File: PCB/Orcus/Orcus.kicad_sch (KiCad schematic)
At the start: 78 parts, among them SW1 MX_LED, SW10 MX_LED, SW11 MX_LED, SW12 MX_LED, SW13 MX_LED, SW14 MX_LED, SW15 MX_LED, SW16 MX_LED, SW17 MX_LED, SW18 MX_LED, SW19 MX_LED, SW2 MX_LED, SW20 MX_LED, SW21 MX_LED, SW22 MX_LED, SW23 MX_LED, SW24 MX_LED, SW25 MX_LED, SW26 MX_LED, SW27 MX_LED, SW28 MX_LED, SW29 MX_LED, SW3 MX_LED, SW30 MX_LED, SW31 MX_LED, SW32 MX_LED, SW33 MX_LED, SW34 MX_LED, SW35 MX_LED, SW36 MX_LED, SW37 MX_LED, SW38 MX_LED, SW4 MX_LED, SW5 MX_LED, SW6 MX_LED, SW7 MX_LED, SW8 MX_LED, SW9 MX_LED, U1 SeeeduinoXIAO, U2 SeeeduinoXIAO

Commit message: update sch
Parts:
- SW1, SW10, SW11, SW12, SW13, SW14, SW15, SW16, SW17, SW18, SW19, SW2, SW20, SW21, SW22, SW23, SW24, SW25, SW26, SW27, SW28, SW29, SW3, SW30, SW31, SW32, SW33, SW34, SW35, SW36, SW37, SW38, SW4, SW5, SW6, SW7, SW8, SW9: footprint Keebio-Parts.pretty-master:Kailh-PG1350-1u-NoLED -> keyswitches.pretty-master:Kailh_socket_PG1350
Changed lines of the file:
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@@
 			)
 		)
-		(property "Footprint" "Keebio-Parts.pretty-master:Kailh-PG1350-1u-NoLED"
+		(property "Footprint" "keyswitches.pretty-master:Kailh_socket_PG1350"
 			(at 53.34 53.34 0)
 			(effects
@@
 			)
 		)
-		(property "Footprint" "Keebio-Parts.pretty-master:Kailh-PG1350-1u-NoLED"
+		(property "Footprint" "keyswitches.pretty-master:Kailh_socket_PG1350"
 			(at 93.98 161.29 0)
 			(effects
@@
 			)
 		)
-		(property "Footprint" "Keebio-Parts.pretty-master:Kailh-PG1350-1u-NoLED"
+		(property "Footprint" "keyswitches.pretty-master:Kailh_socket_PG1350"
 			(at 53.34 35.56 0)
 			(effects
@@
 			)
 		)
-		(property "Footprint" "Keebio-Parts.pretty-master:Kailh-PG1350-1u-NoLED"
+		(property "Footprint" "keyswitches.pretty-master:Kailh_socket_PG1350"
 			(at 74.93 161.29 0)
 			(effects
@@
 			)
 		)
-		(property "Footprint" "Keebio-Parts.pretty-master:Kailh-PG1350-1u-NoLED"
+		(property "Footprint" "keyswitches.pretty-master:Kailh_socket_PG1350"
 			(at 113.03 161.29 0)
 			(effects
@@
 			)
 		)
-		(property "Footprint" "Keebio-Parts.pretty-master:Kailh-PG1350-1u-NoLED"
+		(property "Footprint" "keyswitches.pretty-master:Kailh_socket_PG1350"
 			(at 151.13 142.24 0)
 			(effects
@@
 			)
 		)
-		(property "Footprint" "Keebio-Parts.pretty-master:Kailh-PG1350-1u-NoLED"
+		(property "Footprint" "keyswitches.pretty-master:Kailh_socket_PG1350"
 			(at 130.81 124.46 0)
 			(effects
@@
 			)
 		)
-		(property "Footprint" "Keebio-Parts.pretty-master:Kailh-PG1350-1u-NoLED"
+		(property "Footprint" "keyswitches.pretty-master:Kailh_socket_PG1350"
 			(at 73.66 72.39 0)
 			(effects
@@
 			)
 		)
-		(property "Footprint" "Keebio-Parts.pretty-master:Kailh-PG1350-1u-NoLED"
+		(property "Footprint" "keyswitches.pretty-master:Kailh_socket_PG1350"
 			(at 36.83 181.61 0)
 			(effects
@@
 			)
 		)
-		(property "Footprint" "Keebio-Parts.pretty-master:Kailh-PG1350-1u-NoLED"
+		(property "Footprint" "keyswitches.pretty-master:Kailh_socket_PG1350"
 			(at 147.32 91.44 0)
 			(effects
@@
 			)
 		)
-		(property "Footprint" "Keebio-Parts.pretty-master:Kailh-PG1350-1u-NoLED"
+		(property "Footprint" "keyswitches.pretty-master:Kailh_socket_PG1350"
 			(at 93.98 142.24 0)
 			(effects
@@
 			)
 		)
-		(property "Footprint" "Keebio-Parts.pretty-master:Kailh-PG1350-1u-NoLED"
+		(property "Footprint" "keyswitches.pretty-master:Kailh_socket_PG1350"
 			(at 129.54 35.56 0)
 			(effects
@@
 			)
 		)
-		(property "Footprint" "Keebio-Parts.pretty-master:Kailh-PG1350-1u-NoLED"
+		(property "Footprint" "keyswitches.pretty-master:Kailh_socket_PG1350"
 			(at 111.76 35.56 0)
 			(effects
@@
 			)
 		)
-		(property "Footprint" "Keebio-Parts.pretty-master:Kailh-PG1350-1u-NoLED"
+		(property "Footprint" "keyswitches.pretty-master:Kailh_socket_PG1350"
 			(at 111.76 53.34 0)
 			(effects
@@
 			)
 		)
-		(property "Footprint" "Keebio-Parts.pretty-master:Kailh-PG1350-1u-NoLED"
+		(property "Footprint" "keyswitches.pretty-master:Kailh_socket_PG1350"
 			(at 113.03 142.24 0)
 			(effects
@@
 			)
 		)
-		(property "Footprint" "Keebio-Parts.pretty-master:Kailh-PG1350-1u-NoLED"
+		(property "Footprint" "keyswitches.pretty-master:Kailh_socket_PG1350"
 			(at 129.54 91.44 0)
 			(effects
@@
 			)
 		)
-		(property "Footprint" "Keebio-Parts.pretty-master:Kailh-PG1350-1u-NoLED"
+		(property "Footprint" "keyswitches.pretty-master:Kailh_socket_PG1350"
 			(at 129.54 53.34 0)
 			(effects
@@
 			)
 		)
-		(property "Footprint" "Keebio-Parts.pretty-master:Kailh-PG1350-1u-NoLED"
+		(property "Footprint" "keyswitches.pretty-master:Kailh_socket_PG1350"
 			(at 92.71 72.39 0)
 			(effects
@@
 			)
 		)
-		(property "Footprint" "Keebio-Parts.pretty-master:Kailh-PG1350-1u-NoLED"
+		(property "Footprint" "keyswitches.pretty-master:Kailh_socket_PG1350"
 			(at 31.75 53.34 0)
 			(effects
@@
 			)
 		)
-		(property "Footprint" "Keebio-Parts.pretty-master:Kailh-PG1350-1u-NoLED"
+		(property "Footprint" "keyswitches.pretty-master:Kailh_socket_PG1350"
 			(at 111.76 72.39 0)
 			(effects
@@
 			)
 		)
-		(property "Footprint" "Keebio-Parts.pretty-master:Kailh-PG1350-1u-NoLED"
+		(property "Footprint" "keyswitches.pretty-master:Kailh_socket_PG1350"
 			(at 130.81 161.29 0)
 			(effects
@@
 			)
 		)
-		(property "Footprint" "Keebio-Parts.pretty-master:Kailh-PG1350-1u-NoLED"
+		(property "Footprint" "keyswitches.pretty-master:Kailh_socket_PG1350"
 			(at 129.54 72.39 0)
 			(effects
@@
 			)
 		)
-		(property "Footprint" "Keebio-Parts.pretty-master:Kailh-PG1350-1u-NoLED"
+		(property "Footprint" "keyswitches.pretty-master:Kailh_socket_PG1350"
 			(at 111.76 91.44 0)
 			(effects
@@
 			)
 		)
-		(property "Footprint" "Keebio-Parts.pretty-master:Kailh-PG1350-1u-NoLED"
+		(property "Footprint" "keyswitches.pretty-master:Kailh_socket_PG1350"
 			(at 73.66 35.56 0)
 			(effects
@@
 			)
 		)
-		(property "Footprint" "Keebio-Parts.pretty-master:Kailh-PG1350-1u-NoLED"
+		(property "Footprint" "keyswitches.pretty-master:Kailh_socket_PG1350"
 			(at 72.39 181.61 0)
 			(effects
@@
 			)
 		)
-		(property "Footprint" "Keebio-Parts.pretty-master:Kailh-PG1350-1u-NoLED"
+		(property "Footprint" "keyswitches.pretty-master:Kailh_socket_PG1350"
 			(at 54.61 181.61 0)
 			(effects
@@
 			)
 		)
-		(property "Footprint" "Keebio-Parts.pretty-master:Kailh-PG1350-1u-NoLED"
+		(property "Footprint" "keyswitches.pretty-master:Kailh_socket_PG1350"
 			(at 93.98 124.46 0)
 			(effects
@@
 			)
 		)
-		(property "Footprint" "Keebio-Parts.pretty-master:Kailh-PG1350-1u-NoLED"
+		(property "Footprint" "keyswitches.pretty-master:Kailh_socket_PG1350"
 			(at 54.61 124.46 0)
 			(effects
@@
 			)
 		)
-		(property "Footprint" "Keebio-Parts.pretty-master:Kailh-PG1350-1u-NoLED"
+		(property "Footprint" "keyswitches.pretty-master:Kailh_socket_PG1350"
 			(at 54.61 161.29 0)
 			(effects
@@
 			)
 		)
-		(property "Footprint" "Keebio-Parts.pretty-master:Kailh-PG1350-1u-NoLED"
+		(property "Footprint" "keyswitches.pretty-master:Kailh_socket_PG1350"
 			(at 74.93 124.46 0)
 			(effects
@@
 			)
 		)
-		(property "Footprint" "Keebio-Parts.pretty-master:Kailh-PG1350-1u-NoLED"
+		(property "Footprint" "keyswitches.pretty-master:Kailh_socket_PG1350"
 			(at 113.03 124.46 0)
 			(effects
@@
 			)
 		)
-		(property "Footprint" "Keebio-Parts.pretty-master:Kailh-PG1350-1u-NoLED"
+		(property "Footprint" "keyswitches.pretty-master:Kailh_socket_PG1350"
 			(at 92.71 53.34 0)
 			(effects
@@
 			)
 		)
-		(property "Footprint" "Keebio-Parts.pretty-master:Kailh-PG1350-1u-NoLED"
+		(property "Footprint" "keyswitches.pretty-master:Kailh_socket_PG1350"
 			(at 130.81 142.24 0)
 			(effects
@@
 			)
 		)
-		(property "Footprint" "Keebio-Parts.pretty-master:Kailh-PG1350-1u-NoLED"
+		(property "Footprint" "keyswitches.pretty-master:Kailh_socket_PG1350"
 			(at 92.71 35.56 0)
 			(effects
@@
 			)
 		)
-		(property "Footprint" "Keebio-Parts.pretty-master:Kailh-PG1350-1u-NoLED"
+		(property "Footprint" "keyswitches.pretty-master:Kailh_socket_PG1350"
 			(at 53.34 72.39 0)
 			(effects
@@
 			)
 		)
-		(property "Footprint" "Keebio-Parts.pretty-master:Kailh-PG1350-1u-NoLED"
+		(property "Footprint" "keyswitches.pretty-master:Kailh_socket_PG1350"
 			(at 73.66 53.34 0)
 			(effects
@@
 			)
 		)
-		(property "Footprint" "Keebio-Parts.pretty-master:Kailh-PG1350-1u-NoLED"
+		(property "Footprint" "keyswitches.pretty-master:Kailh_socket_PG1350"
 			(at 54.61 142.24 0)
 			(effects
@@
 			)
 		)
-		(property "Footprint" "Keebio-Parts.pretty-master:Kailh-PG1350-1u-NoLED"
+		(property "Footprint" "keyswitches.pretty-master:Kailh_socket_PG1350"
 			(at 74.93 142.24 0)
 			(effects

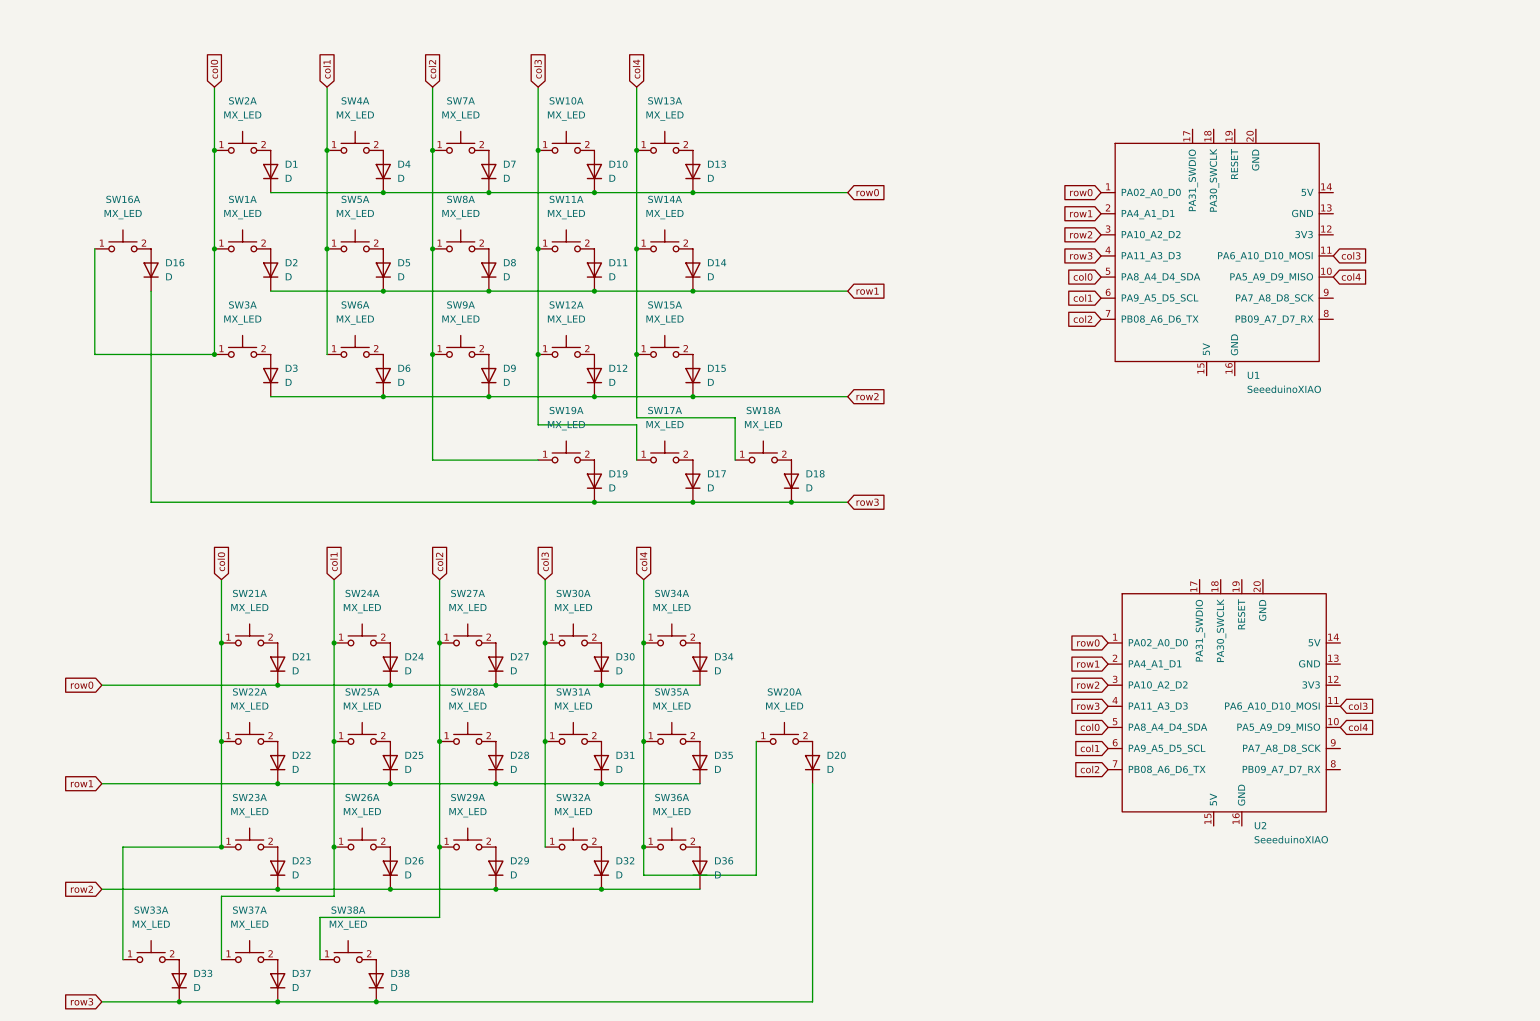
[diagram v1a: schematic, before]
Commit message: footprint laid out
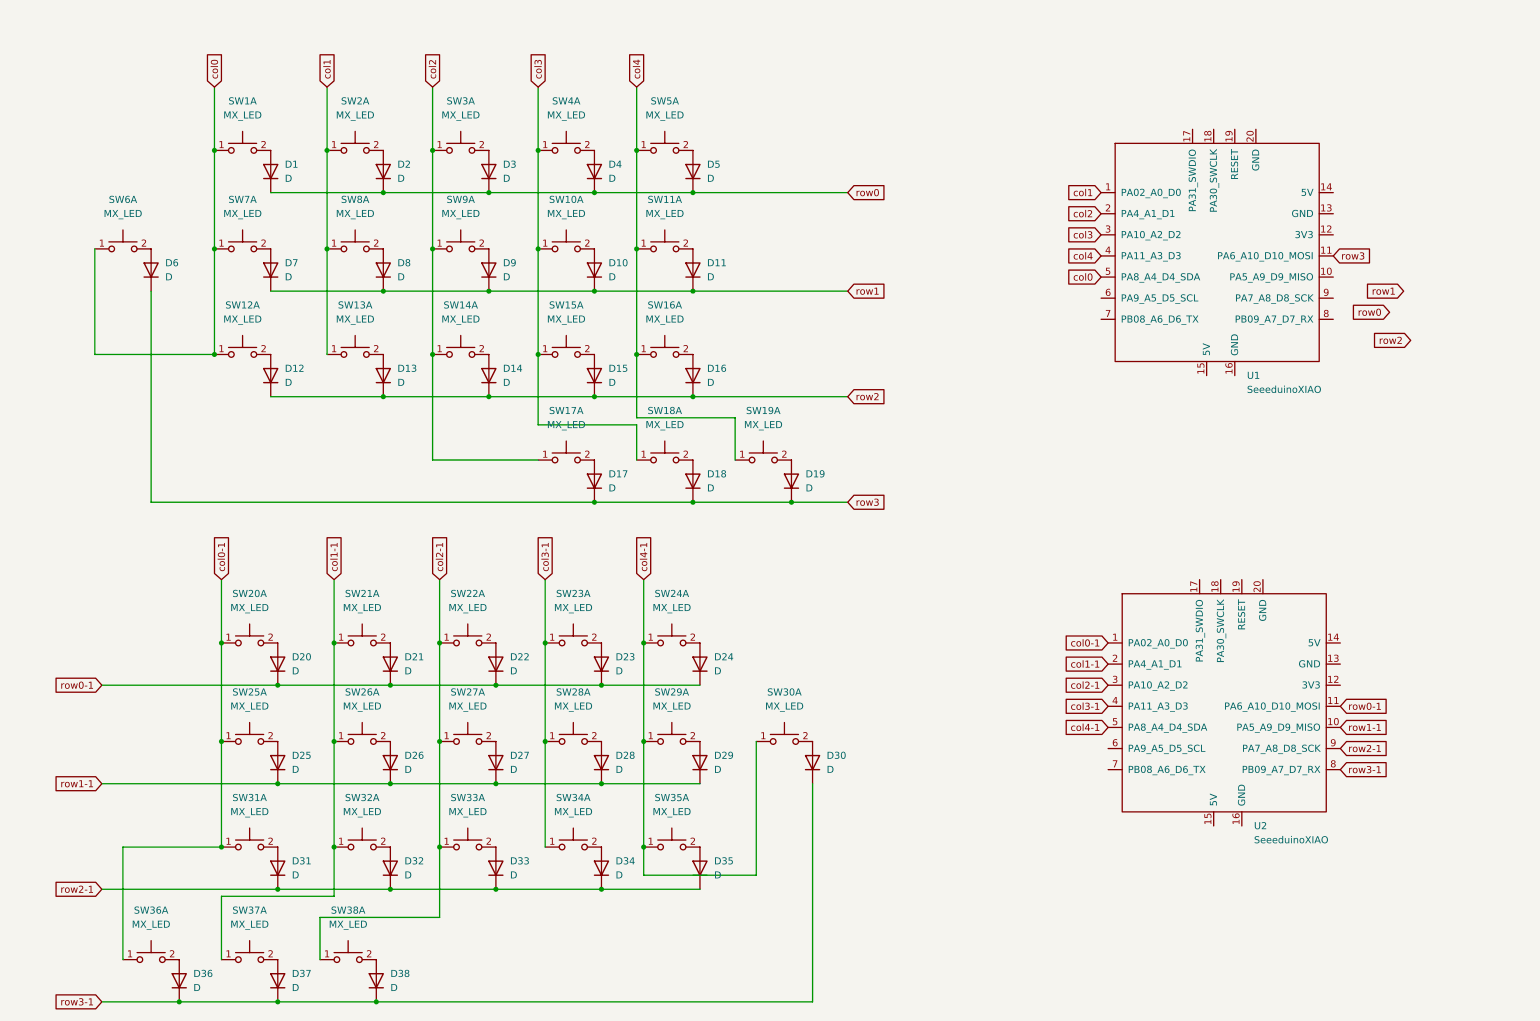
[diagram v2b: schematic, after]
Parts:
- D1, D37, D38: footprint Keebio-Parts.pretty-master:D_SOD123 -> Keebio-Parts.pretty-master:D_SOD123-Hole
- D10: renamed from D11; footprint Keebio-Parts.pretty-master:D_SOD123 -> Keebio-Parts.pretty-master:D_SOD123-Hole
- D11: renamed from D14; footprint Keebio-Parts.pretty-master:D_SOD123 -> Keebio-Parts.pretty-master:D_SOD123-Hole
- D12: renamed from D3; footprint Keebio-Parts.pretty-master:D_SOD123 -> Keebio-Parts.pretty-master:D_SOD123-Hole
- D13: renamed from D6; footprint Keebio-Parts.pretty-master:D_SOD123 -> Keebio-Parts.pretty-master:D_SOD123-Hole
- D14: renamed from D9; footprint Keebio-Parts.pretty-master:D_SOD123 -> Keebio-Parts.pretty-master:D_SOD123-Hole
- D15: renamed from D12; footprint Keebio-Parts.pretty-master:D_SOD123 -> Keebio-Parts.pretty-master:D_SOD123-Hole
- D16: renamed from D15; footprint Keebio-Parts.pretty-master:D_SOD123 -> Keebio-Parts.pretty-master:D_SOD123-Hole
- D17: renamed from D19; footprint Keebio-Parts.pretty-master:D_SOD123 -> Keebio-Parts.pretty-master:D_SOD123-Hole
- D18: renamed from D17; footprint Keebio-Parts.pretty-master:D_SOD123 -> Keebio-Parts.pretty-master:D_SOD123-Hole
- D19: renamed from D18; footprint Keebio-Parts.pretty-master:D_SOD123 -> Keebio-Parts.pretty-master:D_SOD123-Hole
- D2: renamed from D4; footprint Keebio-Parts.pretty-master:D_SOD123 -> Keebio-Parts.pretty-master:D_SOD123-Hole
- D20: renamed from D21; footprint Keebio-Parts.pretty-master:D_SOD123 -> Keebio-Parts.pretty-master:D_SOD123-Hole
- D21: renamed from D24; footprint Keebio-Parts.pretty-master:D_SOD123 -> Keebio-Parts.pretty-master:D_SOD123-Hole
- D22: renamed from D27; footprint Keebio-Parts.pretty-master:D_SOD123 -> Keebio-Parts.pretty-master:D_SOD123-Hole
- D23: renamed from D30; footprint Keebio-Parts.pretty-master:D_SOD123 -> Keebio-Parts.pretty-master:D_SOD123-Hole
- D24: renamed from D34; footprint Keebio-Parts.pretty-master:D_SOD123 -> Keebio-Parts.pretty-master:D_SOD123-Hole
- D25: renamed from D22; footprint Keebio-Parts.pretty-master:D_SOD123 -> Keebio-Parts.pretty-master:D_SOD123-Hole
- D26: renamed from D25; footprint Keebio-Parts.pretty-master:D_SOD123 -> Keebio-Parts.pretty-master:D_SOD123-Hole
- D27: renamed from D28; footprint Keebio-Parts.pretty-master:D_SOD123 -> Keebio-Parts.pretty-master:D_SOD123-Hole
- D28: renamed from D31; footprint Keebio-Parts.pretty-master:D_SOD123 -> Keebio-Parts.pretty-master:D_SOD123-Hole
- D29: renamed from D35; footprint Keebio-Parts.pretty-master:D_SOD123 -> Keebio-Parts.pretty-master:D_SOD123-Hole
- D3: renamed from D7; footprint Keebio-Parts.pretty-master:D_SOD123 -> Keebio-Parts.pretty-master:D_SOD123-Hole
- D30: renamed from D20; footprint Keebio-Parts.pretty-master:D_SOD123 -> Keebio-Parts.pretty-master:D_SOD123-Hole
- D31: renamed from D23; footprint Keebio-Parts.pretty-master:D_SOD123 -> Keebio-Parts.pretty-master:D_SOD123-Hole
- D32: renamed from D26; footprint Keebio-Parts.pretty-master:D_SOD123 -> Keebio-Parts.pretty-master:D_SOD123-Hole
- D33: renamed from D29; footprint Keebio-Parts.pretty-master:D_SOD123 -> Keebio-Parts.pretty-master:D_SOD123-Hole
- D34: renamed from D32; footprint Keebio-Parts.pretty-master:D_SOD123 -> Keebio-Parts.pretty-master:D_SOD123-Hole
- D35: renamed from D36; footprint Keebio-Parts.pretty-master:D_SOD123 -> Keebio-Parts.pretty-master:D_SOD123-Hole
- D36: renamed from D33; footprint Keebio-Parts.pretty-master:D_SOD123 -> Keebio-Parts.pretty-master:D_SOD123-Hole
- D4: renamed from D10; footprint Keebio-Parts.pretty-master:D_SOD123 -> Keebio-Parts.pretty-master:D_SOD123-Hole
- D5: renamed from D13; footprint Keebio-Parts.pretty-master:D_SOD123 -> Keebio-Parts.pretty-master:D_SOD123-Hole
- D6: renamed from D16; footprint Keebio-Parts.pretty-master:D_SOD123 -> Keebio-Parts.pretty-master:D_SOD123-Hole
- D7: renamed from D2; footprint Keebio-Parts.pretty-master:D_SOD123 -> Keebio-Parts.pretty-master:D_SOD123-Hole
- D8: renamed from D5; footprint Keebio-Parts.pretty-master:D_SOD123 -> Keebio-Parts.pretty-master:D_SOD123-Hole
- D9: renamed from D8; footprint Keebio-Parts.pretty-master:D_SOD123 -> Keebio-Parts.pretty-master:D_SOD123-Hole
- SW1: renamed from SW2; footprint keyswitches.pretty-master:Kailh_socket_PG1350 -> Keebio-Parts.pretty-master:Kailh-PG1350-1u-NoLED
- SW10: renamed from SW11; footprint keyswitches.pretty-master:Kailh_socket_PG1350 -> Keebio-Parts.pretty-master:Kailh-PG1350-1u-NoLED
- SW11: renamed from SW14; footprint keyswitches.pretty-master:Kailh_socket_PG1350 -> Keebio-Parts.pretty-master:Kailh-PG1350-1u-NoLED
- SW12: renamed from SW3; footprint keyswitches.pretty-master:Kailh_socket_PG1350 -> Keebio-Parts.pretty-master:Kailh-PG1350-1u-NoLED
- SW13: renamed from SW6; footprint keyswitches.pretty-master:Kailh_socket_PG1350 -> Keebio-Parts.pretty-master:Kailh-PG1350-1u-NoLED
- SW14: renamed from SW9; footprint keyswitches.pretty-master:Kailh_socket_PG1350 -> Keebio-Parts.pretty-master:Kailh-PG1350-1u-NoLED
- SW15: renamed from SW12; footprint keyswitches.pretty-master:Kailh_socket_PG1350 -> Keebio-Parts.pretty-master:Kailh-PG1350-1u-NoLED
- SW16: renamed from SW15; footprint keyswitches.pretty-master:Kailh_socket_PG1350 -> Keebio-Parts.pretty-master:Kailh-PG1350-1u-NoLED
- SW17: renamed from SW19; footprint keyswitches.pretty-master:Kailh_socket_PG1350 -> Keebio-Parts.pretty-master:Kailh-PG1350-1u-NoLED
- SW18: renamed from SW17; footprint keyswitches.pretty-master:Kailh_socket_PG1350 -> Keebio-Parts.pretty-master:Kailh-PG1350-1u-NoLED
- SW19: renamed from SW18; footprint keyswitches.pretty-master:Kailh_socket_PG1350 -> Keebio-Parts.pretty-master:Kailh-PG1350-1u-NoLED
- SW2: renamed from SW4; footprint keyswitches.pretty-master:Kailh_socket_PG1350 -> Keebio-Parts.pretty-master:Kailh-PG1350-1u-NoLED
- SW20: renamed from SW21; footprint keyswitches.pretty-master:Kailh_socket_PG1350 -> Keebio-Parts.pretty-master:Kailh-PG1350-1u-NoLED
- SW21: renamed from SW24; footprint keyswitches.pretty-master:Kailh_socket_PG1350 -> Keebio-Parts.pretty-master:Kailh-PG1350-1u-NoLED
- SW22: renamed from SW27; footprint keyswitches.pretty-master:Kailh_socket_PG1350 -> Keebio-Parts.pretty-master:Kailh-PG1350-1u-NoLED
- SW23: renamed from SW30; footprint keyswitches.pretty-master:Kailh_socket_PG1350 -> Keebio-Parts.pretty-master:Kailh-PG1350-1u-NoLED
- SW24: renamed from SW34; footprint keyswitches.pretty-master:Kailh_socket_PG1350 -> Keebio-Parts.pretty-master:Kailh-PG1350-1u-NoLED
- SW25: renamed from SW22; footprint keyswitches.pretty-master:Kailh_socket_PG1350 -> Keebio-Parts.pretty-master:Kailh-PG1350-1u-NoLED
- SW26: renamed from SW25; footprint keyswitches.pretty-master:Kailh_socket_PG1350 -> Keebio-Parts.pretty-master:Kailh-PG1350-1u-NoLED
- SW27: renamed from SW28; footprint keyswitches.pretty-master:Kailh_socket_PG1350 -> Keebio-Parts.pretty-master:Kailh-PG1350-1u-NoLED
- SW28: renamed from SW31; footprint keyswitches.pretty-master:Kailh_socket_PG1350 -> Keebio-Parts.pretty-master:Kailh-PG1350-1u-NoLED
- SW29: renamed from SW35; footprint keyswitches.pretty-master:Kailh_socket_PG1350 -> Keebio-Parts.pretty-master:Kailh-PG1350-1u-NoLED
- SW3: renamed from SW7; footprint keyswitches.pretty-master:Kailh_socket_PG1350 -> Keebio-Parts.pretty-master:Kailh-PG1350-1u-NoLED
- SW30: renamed from SW20; footprint keyswitches.pretty-master:Kailh_socket_PG1350 -> Keebio-Parts.pretty-master:Kailh-PG1350-1u-NoLED
- SW31: renamed from SW23; footprint keyswitches.pretty-master:Kailh_socket_PG1350 -> Keebio-Parts.pretty-master:Kailh-PG1350-1u-NoLED
- SW32: renamed from SW26; footprint keyswitches.pretty-master:Kailh_socket_PG1350 -> Keebio-Parts.pretty-master:Kailh-PG1350-1u-NoLED
- SW33: renamed from SW29; footprint keyswitches.pretty-master:Kailh_socket_PG1350 -> Keebio-Parts.pretty-master:Kailh-PG1350-1u-NoLED
- SW34: renamed from SW32; footprint keyswitches.pretty-master:Kailh_socket_PG1350 -> Keebio-Parts.pretty-master:Kailh-PG1350-1u-NoLED
- SW35: renamed from SW36; footprint keyswitches.pretty-master:Kailh_socket_PG1350 -> Keebio-Parts.pretty-master:Kailh-PG1350-1u-NoLED
- SW36: renamed from SW33; footprint keyswitches.pretty-master:Kailh_socket_PG1350 -> Keebio-Parts.pretty-master:Kailh-PG1350-1u-NoLED
- SW37, SW38: footprint keyswitches.pretty-master:Kailh_socket_PG1350 -> Keebio-Parts.pretty-master:Kailh-PG1350-1u-NoLED
- SW4: renamed from SW10; footprint keyswitches.pretty-master:Kailh_socket_PG1350 -> Keebio-Parts.pretty-master:Kailh-PG1350-1u-NoLED
- SW5: renamed from SW13; footprint keyswitches.pretty-master:Kailh_socket_PG1350 -> Keebio-Parts.pretty-master:Kailh-PG1350-1u-NoLED
- SW6: renamed from SW16; footprint keyswitches.pretty-master:Kailh_socket_PG1350 -> Keebio-Parts.pretty-master:Kailh-PG1350-1u-NoLED
- SW7: renamed from SW1; footprint keyswitches.pretty-master:Kailh_socket_PG1350 -> Keebio-Parts.pretty-master:Kailh-PG1350-1u-NoLED
- SW8: renamed from SW5; footprint keyswitches.pretty-master:Kailh_socket_PG1350 -> Keebio-Parts.pretty-master:Kailh-PG1350-1u-NoLED
- SW9: renamed from SW8; footprint keyswitches.pretty-master:Kailh_socket_PG1350 -> Keebio-Parts.pretty-master:Kailh-PG1350-1u-NoLED
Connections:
- net col0: no longer SW20.1, SW25.1, SW31.1, SW36.1, U2.5 (PA8_A4_D4_SDA)
- net col1: now also U1.1 (PA02_A0_D0); no longer SW21.1, SW26.1, SW32.1, SW37.1, U1.6 (PA9_A5_D5_SCL), U2.6 (PA9_A5_D5_SCL)
- net col2: now also U1.2 (PA4_A1_D1); no longer SW22.1, SW27.1, SW33.1, SW38.1, U1.7 (PB08_A6_D6_TX), U2.7 (PB08_A6_D6_TX)
- net col3: now also U1.3 (PA10_A2_D2); no longer SW23.1, SW28.1, SW34.1, U1.11 (PA6_A10_D10_MOSI), U2.11 (PA6_A10_D10_MOSI)
- net col4: now also U1.4 (PA11_A3_D3); no longer SW24.1, SW29.1, SW30.1, SW35.1, U1.10 (PA5_A9_D9_MISO), U2.10 (PA5_A9_D9_MISO)
- net row0: no longer D20.1 (K), D21.1 (K), D22.1 (K), D23.1 (K), D24.1 (K), U1.1 (PA02_A0_D0), U2.1 (PA02_A0_D0)
- net row1: no longer D25.1 (K), D26.1 (K), D27.1 (K), D28.1 (K), D29.1 (K), U1.2 (PA4_A1_D1), U2.2 (PA4_A1_D1)
- net row2: no longer D31.1 (K), D32.1 (K), D33.1 (K), D34.1 (K), D35.1 (K), U1.3 (PA10_A2_D2), U2.3 (PA10_A2_D2)
- net row3: now also U1.11 (PA6_A10_D10_MOSI); no longer D30.1 (K), D36.1 (K), D37.1 (K), D38.1 (K), U1.4 (PA11_A3_D3), U2.4 (PA11_A3_D3)
- net row3-1: now reaches U2.8 (PB09_A7_D7_RX)
- net row3-1: now also D30.1 (K), D36.1 (K), D37.1 (K), D38.1 (K)
- net row2-1: now reaches U2.9 (PA7_A8_D8_SCK)
- net row2-1: now also D31.1 (K), D32.1 (K), D33.1 (K), D34.1 (K), D35.1 (K)
- new net col0-1: SW20.1, SW25.1, SW31.1, SW36.1, U2.1 (PA02_A0_D0)
- new net col1-1: SW21.1, SW26.1, SW32.1, SW37.1, U2.2 (PA4_A1_D1)
- new net col2-1: SW22.1, SW27.1, SW33.1, SW38.1, U2.3 (PA10_A2_D2)
- new net col3-1: SW23.1, SW28.1, SW34.1, U2.4 (PA11_A3_D3)
- new net col4-1: SW24.1, SW29.1, SW30.1, SW35.1, U2.5 (PA8_A4_D4_SDA)
- new net row0-1: D20.1 (K), D21.1 (K), D22.1 (K), D23.1 (K), D24.1 (K), U2.11 (PA6_A10_D10_MOSI)
- new net row1-1: D25.1 (K), D26.1 (K), D27.1 (K), D28.1 (K), D29.1 (K), U2.10 (PA5_A9_D9_MISO)
